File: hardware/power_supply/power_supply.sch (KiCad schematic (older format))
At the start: 8 parts, among them J1 Conn_01x04, J2 Conn_01x02, J3 Conn_01x02, U1 LM2596

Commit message: update power supply
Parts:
- removed U1: LM2596, Flypi:LM2596, symbol flypi_components:LM2596
- added U1: LM2596S-5, Package_TO_SOT_THT:TO-220-5_P3.4x3.7mm_StaggerOdd_Lead3.8mm_Vertical, symbol Regulator_Switching:LM2596S-5
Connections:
- wire segments 35 -> 39
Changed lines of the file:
@@
 EESchema Schematic File Version 4
-LIBS:power_supply-cache
 EELAYER 30 0
 EELAYER END
@@
 $EndComp
 $Comp
-L flypi_components:LM2596 U1
-U 1 1 5E26A79A
-P 5300 2650
-F 0 "U1" H 5325 2853 60  0000 C CNN
-F 1 "LM2596" H 5325 2747 60  0000 C CNN
-F 2 "Flypi:LM2596" H 5325 2641 60  0000 C CNN
-F 3 "" H 5500 2650 60  0000 C CNN
-	1    5300 2650
-	1    0    0    -1
-$EndComp
-$Comp
 L Device:D_Schottky D1
 U 1 1 5E26BBB5
@@
 Connection ~ 4750 3000
 Wire Wire Line
-	4750 3000 4900 3000
-Wire Wire Line
 	4750 2300 5200 2300
-$Comp
-L power:GND #PWR01
-U 1 1 5E26D43B
-P 4750 3550
-F 0 "#PWR01" H 4750 3300 50  0001 C CNN
-F 1 "GND" H 4755 3377 50  0000 C CNN
-F 2 "" H 4750 3550 50  0001 C CNN
-F 3 "" H 4750 3550 50  0001 C CNN
-	1    4750 3550
-	1    0    0    -1
-$EndComp
 Wire Wire Line
 	4750 3000 4750 3200
-Wire Wire Line
-	4750 3200 4900 3200
 Connection ~ 4750 3200
 Wire Wire Line
-	5750 2900 5750 2300
-Wire Wire Line
-	5750 2300 5500 2300
-Wire Wire Line
 	4300 2800 4200 2800
 Wire Wire Line
 	4200 2800 4200 2650
 Wire Wire Line
-	4200 2650 4900 2650
-Wire Wire Line
-	4900 2650 4900 2800
-Wire Wire Line
 	3850 3200 4750 3200
-Wire Wire Line
-	4750 3550 4750 3400
 $Comp
 L Device:CP C2
@@
 	1    0    0    -1
 $EndComp
-Wire Wire Line
-	5750 3100 6250 3100
-Wire Wire Line
-	6250 3400 4750 3400
-Connection ~ 4750 3400
-Wire Wire Line
-	4750 3400 4750 3200
 $Comp
 L Device:L L1
@@
 $EndComp
 Wire Wire Line
-	5750 2300 5850 2300
-Connection ~ 5750 2300
-Wire Wire Line
 	6150 2300 6250 2300
 Wire Wire Line
@@
 $EndComp
 Text Notes 8750 2600 2    100  ~ 0
+DATA 2
+Text Notes 8750 2400 2    100  ~ 0
+DATA 1
+Text Notes 8750 2800 2    100  ~ 0
+VCC
+Text Notes 8750 3000 2    100  ~ 0
 GND
-Text Notes 8750 2400 2    100  ~ 0
-VCC
-Text Notes 8750 2800 2    100  ~ 0
-DATA 2
-Text Notes 8750 3000 2    100  ~ 0
-DATA 1
 Wire Notes Line style solid
 	8800 3050 8150 3050
@@
 Wire Notes Line
 	6600 1700 6600 3300
-Wire Wire Line
-	6750 2850 7100 2850
-Wire Wire Line
-	6900 2300 6900 2750
 $Comp
 L Connector_Generic:Conn_01x04 J1
@@
 $EndComp
 Wire Wire Line
-	3300 2850 3850 2850
-Wire Wire Line
-	3850 2850 3850 3200
-Wire Wire Line
-	3300 2750 4000 2750
-Wire Wire Line
-	4000 2750 4000 2800
-Wire Wire Line
 	4000 2800 4200 2800
 Connection ~ 4200 2800
-NoConn ~ 3300 2950
-NoConn ~ 3300 3050
-Wire Wire Line
-	6900 2300 7100 2300
+NoConn ~ 3300 2850
+$Comp
+L Regulator_Switching:LM2596S-5 U1
+U 1 1 5F3FE20F
+P 5350 3200
+F 0 "U1" H 5350 3567 50  0000 C CNN
+F 1 "LM2596S-5" H 5350 3476 50  0000 C CNN
+F 2 "Package_TO_SOT_THT:TO-220-5_P3.4x3.7mm_StaggerOdd_Lead3.8mm_Vertical" H 5400 2950 50  0001 L CIN
+F 3 "http://www.ti.com/lit/ds/symlink/lm2596.pdf" H 5350 3200 50  0001 C CNN
+	1    5350 3200
+	1    0    0    -1
+$EndComp
+Wire Wire Line
+	4750 3200 4750 3300
+$Comp
+L power:GND #PWR03
+U 1 1 5F403948
+P 6250 3550
+F 0 "#PWR03" H 6250 3300 50  0001 C CNN
+F 1 "GND" H 6255 3377 50  0000 C CNN
+F 2 "" H 6250 3550 50  0001 C CNN
+F 3 "" H 6250 3550 50  0001 C CNN
+	1    6250 3550
+	1    0    0    -1
+$EndComp
+Wire Wire Line
+	5750 2300 5850 2300
+Wire Wire Line
+	5750 2300 5500 2300
+Connection ~ 5750 2300
+Wire Wire Line
+	5750 2700 5950 2700
+Wire Wire Line
+	5950 2700 5950 3300
+Wire Wire Line
+	5750 2700 5750 2300
+Wire Wire Line
+	5850 3100 6250 3100
+Wire Wire Line
+	6250 3400 6250 3550
+Wire Wire Line
+	5950 3300 5850 3300
+Wire Wire Line
+	4850 2650 4850 3100
+Wire Wire Line
+	4200 2650 4850 2650
+Wire Wire Line
+	4850 3300 4750 3300
+Connection ~ 4750 3300
+Wire Wire Line
+	4750 3300 4750 3500
+Wire Wire Line
+	5350 3500 4750 3500
+Connection ~ 4750 3500
+Wire Wire Line
+	4750 3500 4750 3550
+$Comp
+L power:GND #PWR01
+U 1 1 5F409BB8
+P 4750 3550
+F 0 "#PWR01" H 4750 3300 50  0001 C CNN
+F 1 "GND" H 4755 3377 50  0000 C CNN
+F 2 "" H 4750 3550 50  0001 C CNN
+F 3 "" H 4750 3550 50  0001 C CNN
+	1    4750 3550
+	1    0    0    -1
+$EndComp
+Wire Wire Line
+	6900 2300 6900 2750
 Wire Wire Line
 	6750 2300 6750 2400
-Connection ~ 6750 2400
-Wire Wire Line
-	7100 2400 6750 2400
-Wire Wire Line
-	6750 2400 6750 2850
 Wire Wire Line
 	7100 2750 6900 2750
@@
 Wire Wire Line
 	6900 2750 6900 3550
+Wire Wire Line
+	7100 2300 6900 2300
+Wire Wire Line
+	7100 2400 6750 2400
+Connection ~ 6750 2400
+Wire Wire Line
+	6750 2400 6750 2850
+Wire Wire Line
+	7100 2850 6750 2850
+Wire Wire Line
+	3850 3050 3300 3050
+Wire Wire Line
+	3850 3050 3850 3200
+Wire Wire Line
+	3300 2950 4000 2950
+Wire Wire Line
+	4000 2950 4000 2800
+NoConn ~ 3300 2750
 $EndSCHEMATC

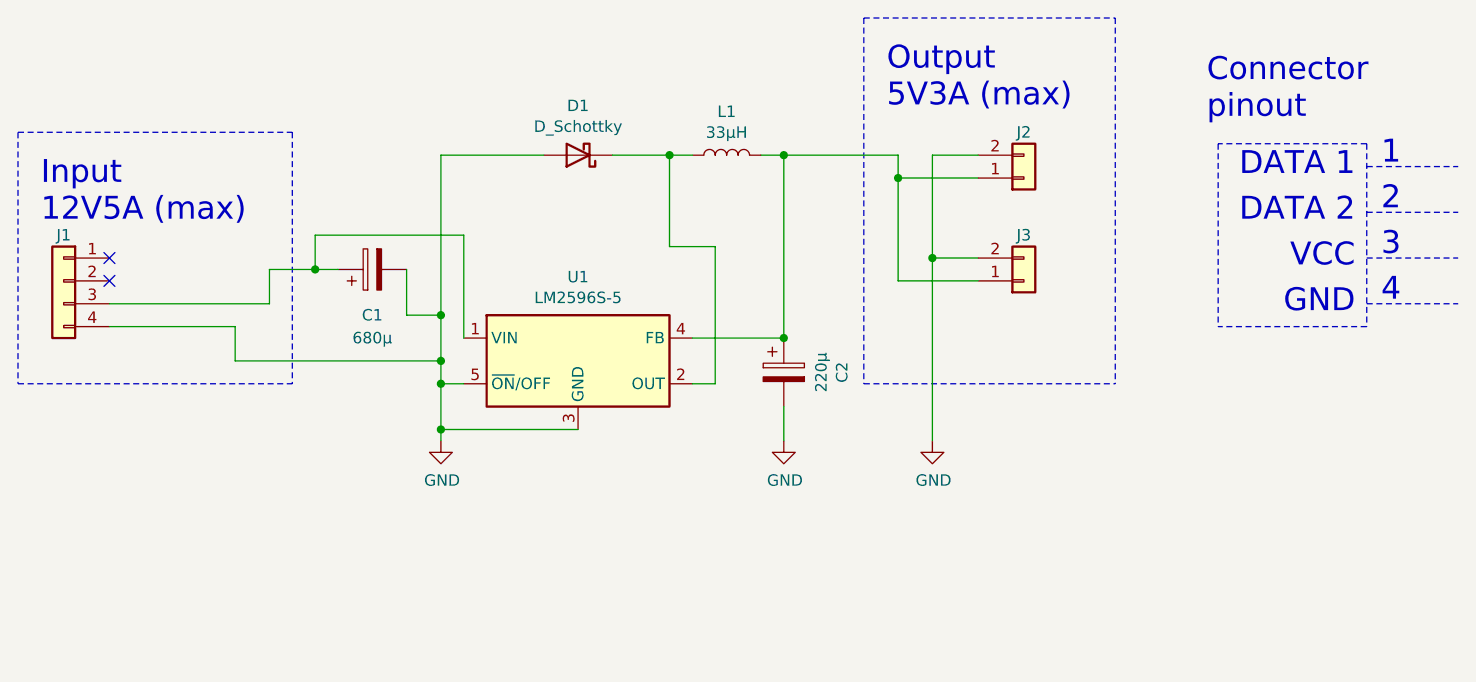
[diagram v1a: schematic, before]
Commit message: Update on 12V5A system power line
- 12V5A power line is now represented by two connectors with 2 pins across all the modules
- all .png previews are updated. The central hub now has previews for schematics, PCB tracing and 3D model
- peltier module now has two 12V5A connectors with redesigned one side of the bridge. Now all MOSFETs can be equipped with heatsinks
- hum/temp sensor now has its connector position reversed to mimic Grove's one
- hum/temp and gas sensors now have a small BeeHive logo on front layer rather than one big on back layer
- hum/temp sensor now use only one layer for signals and one layer for ground
- switch arrays now have two connectors for 12V5A and 5V3A power lines
- switch arrays had their power lines better traced (no sharp turns)
- power supply (12V5A to 5V3A) now has two connectors for 12V5A power line
- one trace of power supply, which lies in between LM2596's legs, was narrowed to ensure that it will not be accidentally soldered or damaged during placement
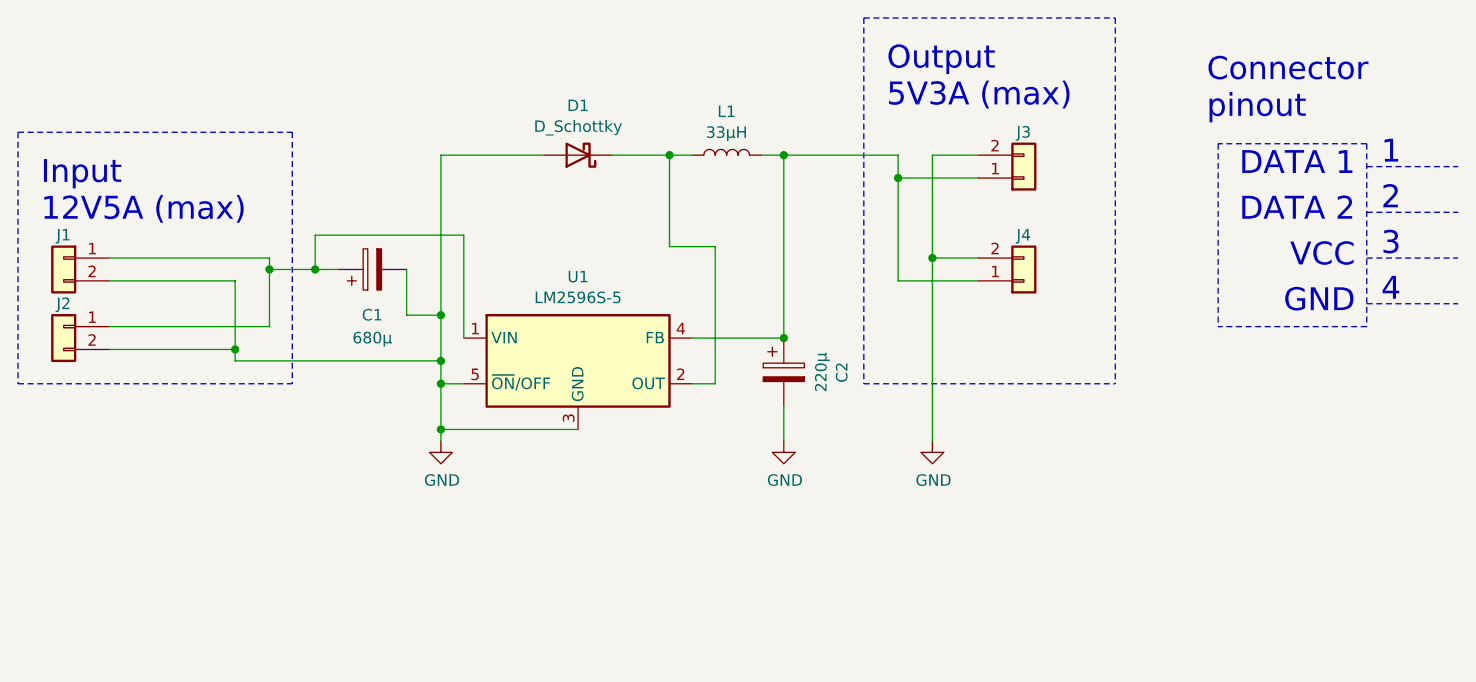
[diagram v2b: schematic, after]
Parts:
- removed J1: Conn_01x04, Connector_JST:JST_XH_B4B-XH-A_1x04_P2.50mm_Vertical, symbol Connector_Generic:Conn_01x04
- added J1, J2: Conn_01x02, Connector_JST:JST_XH_B2B-XH-A_1x02_P2.50mm_Vertical, symbol Connector_Generic:Conn_01x02
- renumbered J2 to J3, J3 to J4
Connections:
- net GND: now also J1.2 (Pin_2), J2.2 (Pin_2)
- net at C1.1, U1.1 (VIN): now also J1.1 (Pin_1), J2.1 (Pin_1)
- no-connect marks 2 -> 0
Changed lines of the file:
@@
 Connection ~ 6250 3100
 $Comp
-L Connector_Generic:Conn_01x02 J2
+L Connector_Generic:Conn_01x02 J3
 U 1 1 5E277019
 P 7300 2400
-F 0 "J2" H 7300 2200 50  0000 C CNN
+F 0 "J3" H 7300 2200 50  0000 C CNN
 F 1 "Conn_01x02" H 7218 2166 50  0001 C CNN
 F 2 "Connector_JST:JST_XH_B2B-XH-A_1x02_P2.50mm_Vertical" H 7300 2400 50  0001 C CNN
@@
 $EndComp
 $Comp
-L Connector_Generic:Conn_01x02 J3
+L Connector_Generic:Conn_01x02 J4
 U 1 1 5E277D0A
 P 7300 2850
-F 0 "J3" H 7300 2650 50  0000 C CNN
+F 0 "J4" H 7300 2650 50  0000 C CNN
 F 1 "Conn_01x02" H 7218 2616 50  0001 C CNN
 F 2 "Connector_JST:JST_XH_B2B-XH-A_1x02_P2.50mm_Vertical" H 7300 2850 50  0001 C CNN
@@
 Wire Notes Line
 	6600 1700 6600 3300
-$Comp
-L Connector_Generic:Conn_01x04 J1
-U 1 1 5E26F9D6
-P 3100 2850
-F 0 "J1" H 3100 3050 50  0000 C CNN
-F 1 "Conn_01x04" H 3000 2550 50  0001 C CNN
-F 2 "Connector_JST:JST_XH_B4B-XH-A_1x04_P2.50mm_Vertical" H 3100 2850 50  0001 C CNN
-F 3 "~" H 3100 2850 50  0001 C CNN
-	1    3100 2850
-	-1   0    0    -1
-$EndComp
 Wire Wire Line
 	4000 2800 4200 2800
 Connection ~ 4200 2800
-NoConn ~ 3300 2850
 $Comp
 L Regulator_Switching:LM2596S-5 U1
@@
 	7100 2850 6750 2850
 Wire Wire Line
-	3850 3050 3300 3050
-Wire Wire Line
-	3850 3050 3850 3200
-Wire Wire Line
-	3300 2950 4000 2950
-Wire Wire Line
-	4000 2950 4000 2800
-NoConn ~ 3300 2750
+	3850 3150 3300 3150
+Wire Wire Line
+	3300 3050 4000 3050
+$Comp
+L Connector_Generic:Conn_01x02 J2
+U 1 1 5FD2430D
+P 3100 3050
+F 0 "J2" H 3100 3150 50  0000 C CNN
+F 1 "Conn_01x02" V 3250 3000 50  0001 C CNN
+F 2 "Connector_JST:JST_XH_B2B-XH-A_1x02_P2.50mm_Vertical" H 3100 3050 50  0001 C CNN
+F 3 "~" H 3100 3050 50  0001 C CNN
+	1    3100 3050
+	-1   0    0    -1
+$EndComp
+$Comp
+L Connector_Generic:Conn_01x02 J1
+U 1 1 5FD2538D
+P 3100 2750
+F 0 "J1" H 3100 2850 50  0000 C CNN
+F 1 "Conn_01x02" V 3250 2700 50  0001 C CNN
+F 2 "Connector_JST:JST_XH_B2B-XH-A_1x02_P2.50mm_Vertical" H 3100 2750 50  0001 C CNN
+F 3 "~" H 3100 2750 50  0001 C CNN
+	1    3100 2750
+	-1   0    0    -1
+$EndComp
+Wire Wire Line
+	3850 3150 3850 3200
+Wire Wire Line
+	4000 2800 4000 3050
+Wire Wire Line
+	3300 2750 4000 2750
+Wire Wire Line
+	4000 2750 4000 2800
+Connection ~ 4000 2800
+Wire Wire Line
+	3300 2850 3850 2850
+Wire Wire Line
+	3850 2850 3850 3150
+Connection ~ 3850 3150
 $EndSCHEMATC

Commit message: Update 5V3A breakout
- added LED for 12V5A line;
- added two 5V3A line connectors added;
- implemented board version as text marking on PCB;
- changed the size of PCB to match others;
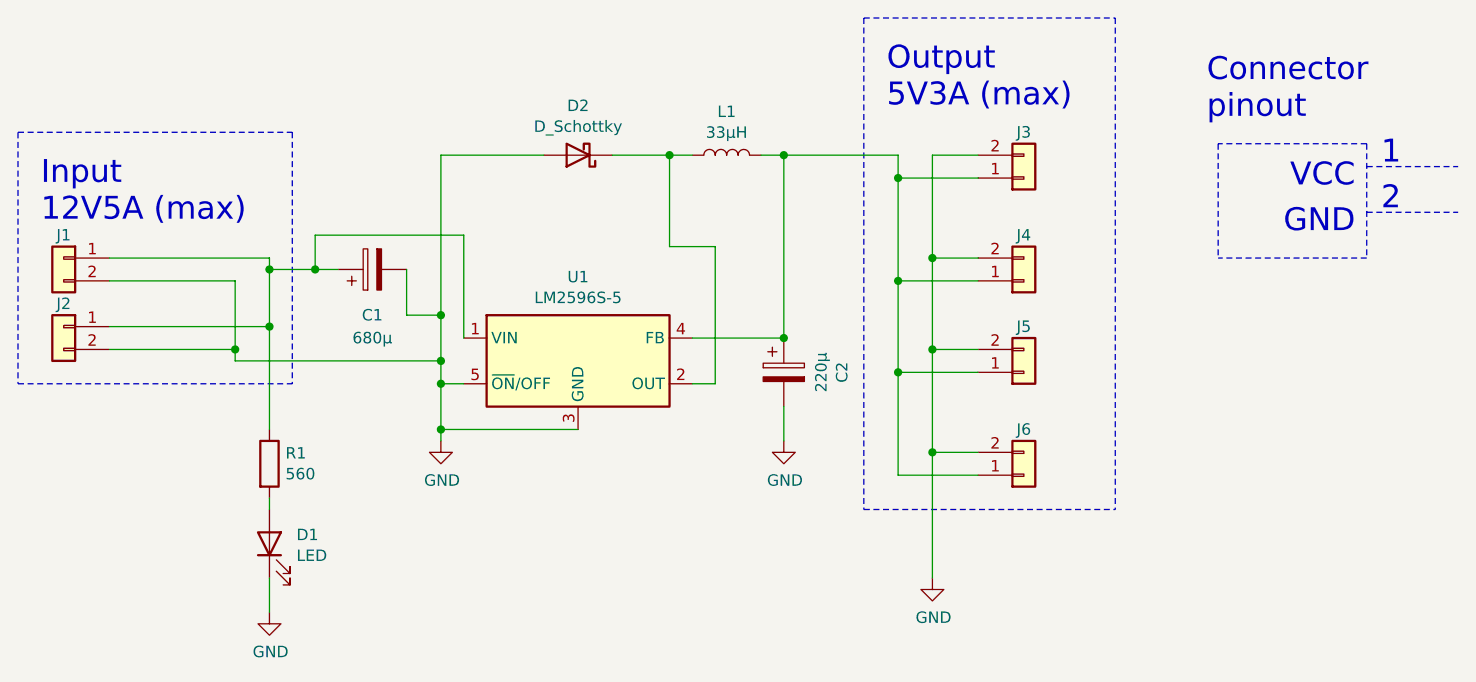
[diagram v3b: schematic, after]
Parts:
- added D1: LED, LED_THT:LED_D3.0mm, symbol Device:LED
- added J5, J6: Conn_01x02, Connector_JST:JST_XH_B2B-XH-A_1x02_P2.50mm_Vertical, symbol Connector_Generic:Conn_01x02
- added R1: 560, Resistor_THT:R_Box_L13.0mm_W4.0mm_P9.00mm, symbol Device:R
- renumbered D1 to D2
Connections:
- net GND: now also D1.1 (K), J5.2 (Pin_2), J6.2 (Pin_2)
- net at C1.1, J1.1 (Pin_1), J2.1 (Pin_1)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: now also R1.1
- net at C2.1, J3.1 (Pin_1), J4.1 (Pin_1)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: now also J5.1 (Pin_1), J6.1 (Pin_1)
- new net: D1.2 (A), R1.2
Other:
- note removed: "3"
- note removed: "4"
- note removed: "DATA 1"
- note removed: "DATA 2"
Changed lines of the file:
@@
 $EndComp
 $Comp
-L Device:D_Schottky D1
+L Device:D_Schottky D2
 U 1 1 5E26BBB5
 P 5350 2300
-F 0 "D1" H 5350 2084 50  0000 C CNN
+F 0 "D2" H 5350 2084 50  0000 C CNN
 F 1 "D_Schottky" H 5350 2175 50  0000 C CNN
 F 2 "Diode_THT:D_DO-201_P15.24mm_Horizontal" H 5350 2300 50  0001 C CNN
@@
 L power:GND #PWR02
 U 1 1 5E278D9D
-P 6900 3550
-F 0 "#PWR02" H 6900 3300 50  0001 C CNN
-F 1 "GND" H 6905 3377 50  0000 C CNN
-F 2 "" H 6900 3550 50  0001 C CNN
-F 3 "" H 6900 3550 50  0001 C CNN
-	1    6900 3550
-	1    0    0    -1
-$EndComp
-Text Notes 8750 2600 2    100  ~ 0
-DATA 2
-Text Notes 8750 2400 2    100  ~ 0
-DATA 1
-Text Notes 8750 2800 2    100  ~ 0
+P 6900 4150
+F 0 "#PWR02" H 6900 3900 50  0001 C CNN
+F 1 "GND" H 6905 3977 50  0000 C CNN
+F 2 "" H 6900 4150 50  0001 C CNN
+F 3 "" H 6900 4150 50  0001 C CNN
+	1    6900 4150
+	1    0    0    -1
+$EndComp
+Text Notes 8750 2450 2    100  ~ 0
 VCC
-Text Notes 8750 3000 2    100  ~ 0
+Text Notes 8750 2650 2    100  ~ 0
 GND
 Wire Notes Line style solid
-	8800 3050 8150 3050
+	8800 2750 8150 2750
 Wire Notes Line style solid
 	8800 2250 8150 2250
-Wire Notes Line style solid
-	8150 2250 8150 3050
-Wire Notes Line style solid
-	8800 2250 8800 3050
-Wire Notes Line style solid
-	8800 2950 9200 2950
-Wire Notes Line style solid
-	8800 2750 9200 2750
 Wire Notes Line style solid rgb(255, 0, 0)
 	8800 2350 9200 2350
@@
 Text Notes 8950 2550 2    100  ~ 0
 2
-Text Notes 8950 2750 2    100  ~ 0
-3
-Text Notes 8950 2950 2    100  ~ 0
-4
 Text Notes 8100 2150 0    100  ~ 0
 Connector\npinout
@@
 	6600 1700 7700 1700
 Wire Notes Line
-	6600 3300 7700 3300
+	6600 3850 7700 3850
 Wire Notes Line
 	2900 2200 4100 2200
 Wire Notes Line
 	2900 3300 4100 3300
-Wire Notes Line
-	7700 1700 7700 3300
-Wire Notes Line
-	6600 1700 6600 3300
 Wire Wire Line
 	4000 2800 4200 2800
@@
 Connection ~ 6900 2750
 Wire Wire Line
-	6900 2750 6900 3550
+	6900 2750 6900 3150
 Wire Wire Line
 	7100 2300 6900 2300
@@
 	3850 2850 3850 3150
 Connection ~ 3850 3150
+$Comp
+L Device:R R1
+U 1 1 60292F3D
+P 4000 3650
+F 0 "R1" H 4070 3696 50  0000 L CNN
+F 1 "560" H 4070 3605 50  0000 L CNN
+F 2 "Resistor_THT:R_Box_L13.0mm_W4.0mm_P9.00mm" V 3930 3650 50  0001 C CNN
+F 3 "~" H 4000 3650 50  0001 C CNN
+	1    4000 3650
+	1    0    0    -1
+$EndComp
+Wire Wire Line
+	4000 3500 4000 3050
+Connection ~ 4000 3050
+$Comp
+L Device:LED D1
+U 1 1 602950A0
+P 4000 4000
+F 0 "D1" V 4039 3882 50  0000 R CNN
+F 1 "LED" V 3948 3882 50  0000 R CNN
+F 2 "LED_THT:LED_D3.0mm" H 4000 4000 50  0001 C CNN
+F 3 "~" H 4000 4000 50  0001 C CNN
+	1    4000 4000
+	0    -1   -1   0
+$EndComp
+Wire Wire Line
+	4000 3800 4000 3850
+$Comp
+L power:GND #PWR0101
+U 1 1 60296335
+P 4000 4300
+F 0 "#PWR0101" H 4000 4050 50  0001 C CNN
+F 1 "GND" H 4005 4127 50  0000 C CNN
+F 2 "" H 4000 4300 50  0001 C CNN
+F 3 "" H 4000 4300 50  0001 C CNN
+	1    4000 4300
+	1    0    0    -1
+$EndComp
+Wire Wire Line
+	4000 4150 4000 4300
+$Comp
+L Connector_Generic:Conn_01x02 J5
+U 1 1 602991BE
+P 7300 3250
+F 0 "J5" H 7300 3050 50  0000 C CNN
+F 1 "Conn_01x02" H 7218 3016 50  0001 C CNN
+F 2 "Connector_JST:JST_XH_B2B-XH-A_1x02_P2.50mm_Vertical" H 7300 3250 50  0001 C CNN
+F 3 "~" H 7300 3250 50  0001 C CNN
+	1    7300 3250
+	1    0    0    1
+$EndComp
+$Comp
+L Connector_Generic:Conn_01x02 J6
+U 1 1 602991C4
+P 7300 3700
+F 0 "J6" H 7300 3500 50  0000 C CNN
+F 1 "Conn_01x02" H 7218 3466 50  0001 C CNN
+F 2 "Connector_JST:JST_XH_B2B-XH-A_1x02_P2.50mm_Vertical" H 7300 3700 50  0001 C CNN
+F 3 "~" H 7300 3700 50  0001 C CNN
+	1    7300 3700
+	1    0    0    1
+$EndComp
+Wire Wire Line
+	6750 2850 6750 3250
+Wire Wire Line
+	6750 3250 7100 3250
+Connection ~ 6750 2850
+Wire Wire Line
+	6750 3250 6750 3700
+Wire Wire Line
+	6750 3700 7100 3700
+Connection ~ 6750 3250
+Wire Wire Line
+	7100 3600 6900 3600
+Connection ~ 6900 3600
+Wire Wire Line
+	6900 3600 6900 4150
+Wire Wire Line
+	7100 3150 6900 3150
+Connection ~ 6900 3150
+Wire Wire Line
+	6900 3150 6900 3600
+Wire Notes Line
+	7700 1700 7700 3850
+Wire Notes Line
+	6600 1700 6600 3850
+Wire Notes Line style solid
+	8150 2250 8150 2750
+Wire Notes Line style solid
+	8800 2250 8800 2750
 $EndSCHEMATC
